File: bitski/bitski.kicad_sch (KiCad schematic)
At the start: 9 parts, among them J2 USB_C_Receptacle_USB2.0_16P, U1 ESP32-S3-MINI-1-N8, U2 BQ25185

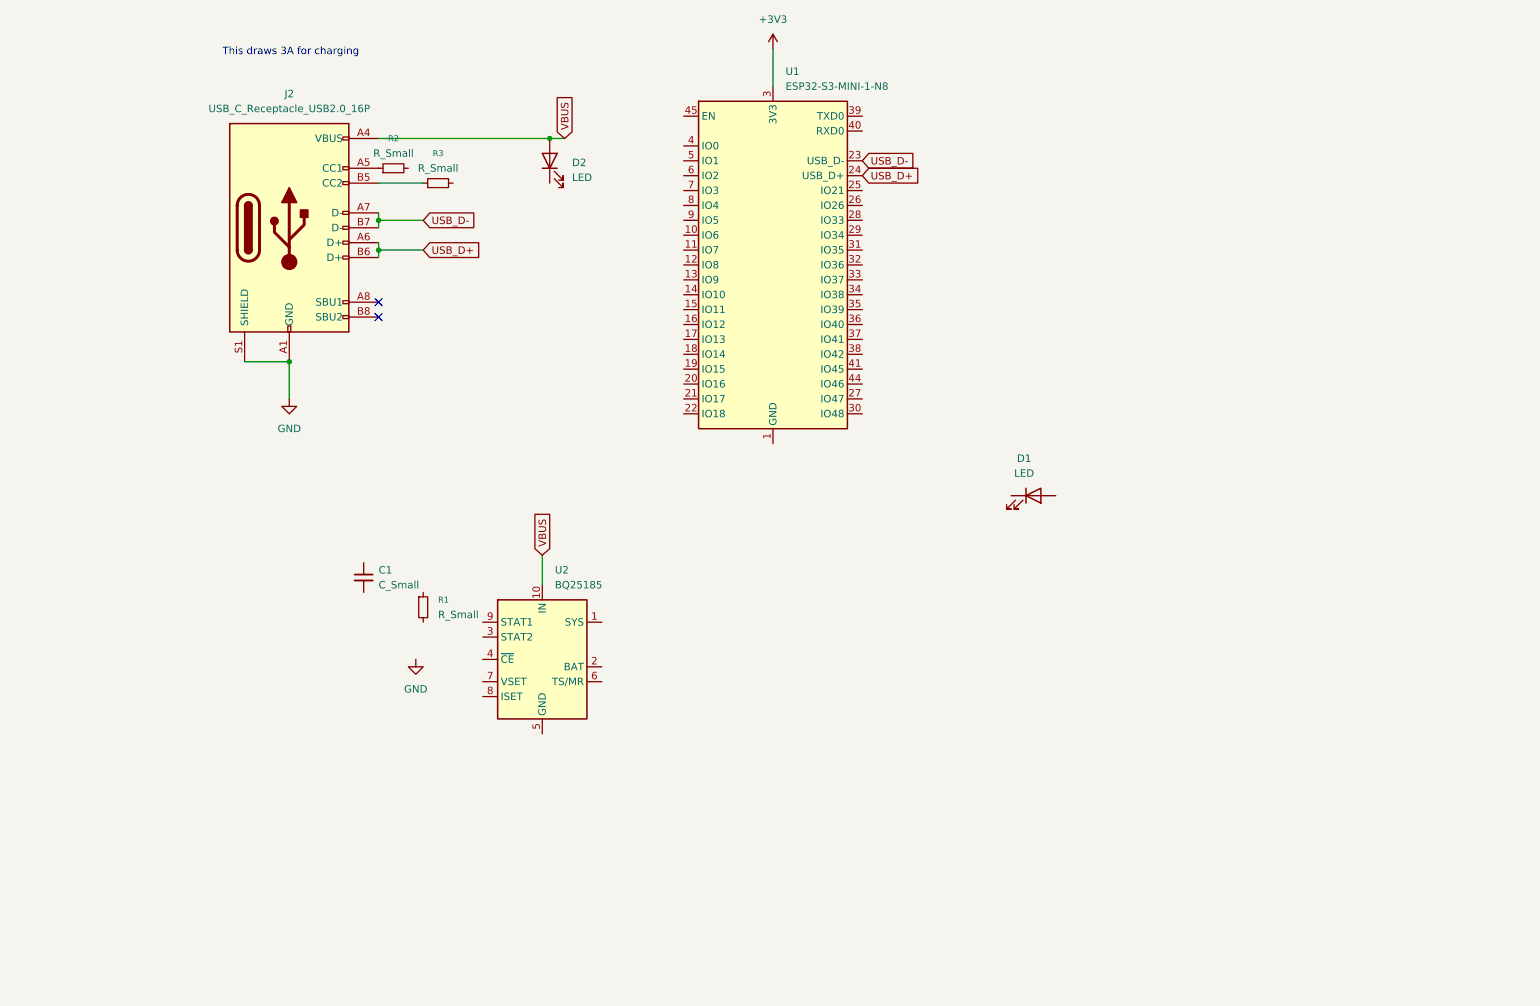
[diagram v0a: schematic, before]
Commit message: updated schematic, added gitignore
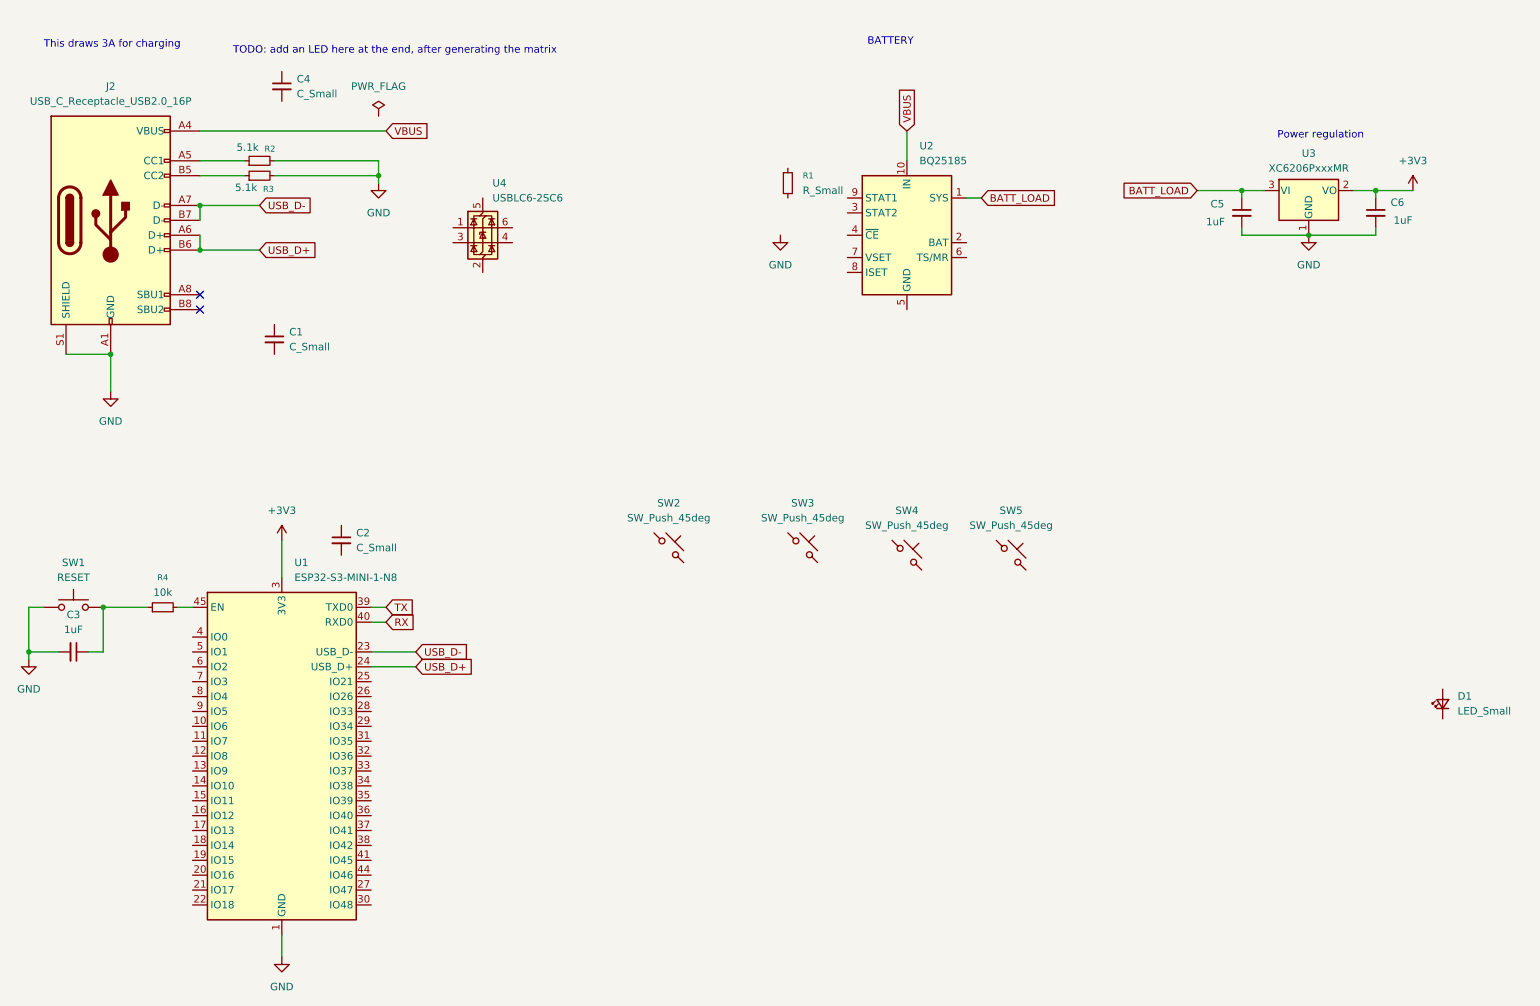
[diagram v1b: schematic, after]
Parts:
- removed D1, D2: LED, symbol Device:LED
- added C2, C4: C_Small, symbol Device:C_Small
- added C3, C5, C6: 1uF, symbol Device:C_Small
- added D1: LED_Small, symbol Device:LED_Small
- added R4: 10k, symbol Device:R_Small
- added SW1: RESET, symbol Switch:SW_Push
- added SW2, SW3, SW4, SW5: SW_Push_45deg, symbol Switch:SW_Push_45deg
- added U3: XC6206PxxxMR, Package_TO_SOT_SMD:SOT-23-3, symbol Regulator_Linear:XC6206PxxxMR
- added U4: USBLC6-2SC6, Package_TO_SOT_SMD:SOT-23-6, symbol Power_Protection:USBLC6-2SC6
- R2, R3: value R_Small -> 5.1k
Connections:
- net +3V3: now also C6.1, U3.2 (VO)
- net GND: now also R2.2, R3.2, U1.1 (GND), U1.2 (GND), U1.42 (GND), U1.43 (GND), U1.46 (GND), U1.47 (GND), U1.48 (GND), U1.49 (GND), U1.50 (GND), U1.51 (GND), U1.52 (GND), U1.53 (GND), U1.54 (GND), U1.55 (GND), U1.56 (GND), U1.57 (GND), U1.58 (GND), U1.59 (GND), U1.60 (GND), U1.61 (GND), U1.62 (GND), U1.63 (GND), U1.64 (GND), U1.65 (GND), C3.2, C5.2, C6.2, SW1.1, U3.1 (GND)
- net TX: now reaches U1.39 (TXD0)
- net RX: now reaches U1.40 (RXD0)
- net at U1.45 (EN): now also R4.2
- net BATT_LOAD: now reaches U2.1 (SYS)
- net BATT_LOAD: now also C5.1, U3.3 (VI)
- new net: C3.1, R4.1, SW1.2
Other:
- note added: "BATTERY"
- note added: "Power regulation"
- note added: "TODO: add an LED here at the end, after generating the matrix"
- moved on the sheet: C1, J2, R1, R2, R3, U1, U2

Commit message: updated board waow
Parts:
- removed C1, C2, C4: C_Small, symbol Device:C_Small
- removed D1: LED_Small, symbol Device:LED_Small
- removed R1: R_Small, symbol Device:R_Small
- removed R2, R3: 5.1k, symbol Device:R_Small
- added C7, C8: 0pF, symbol Device:C_Small
- added D2: D_Schottky, symbol Device:D_Schottky
- added D3, D4, D5, D6: LED_45deg, LED_SMD:LED_0402_1005Metric, symbol Device:LED_45deg
- added J1: Conn_02x20_Odd_Even, symbol Connector_Generic:Conn_02x20_Odd_Even
- added JP1: Jumper_2_Small_Bridged, symbol Jumper:Jumper_2_Small_Bridged
- added R2: 5.1k, Resistor_SMD:R_0402_1005Metric, symbol Device:R
- added R3: 5.1k, symbol Device:R
- added R5, R6: 33, symbol Device:R
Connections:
- net GND: now also SW2.2, SW3.2, SW4.2, SW5.2, U2.5 (GND), U4.2 (GND), C7.2, C8.2, R2.2, R3.2
- net VBUS: now also U4.5 (VBUS), D2.2 (A); no longer U2.10 (IN)
- net USB_DM: now reaches U4.1 (I/O1)
- net USB_DM: now also J2.A7 (D-), J2.B7 (D-)
- net USB_DP: now reaches U4.3 (I/O2)
- net USB_DP: now also J2.A6 (D+), J2.B6 (D+)
- net at U4.4 (I/O2): now also C7.1, R6.1
- net at U4.6 (I/O1): now also C8.1, R5.1
- net at J2.B5 (CC2): now also R3.1
- net at J2.A5 (CC1): now also R2.1
- net INPUT4: now reaches SW5.1
- net INPUT1: now reaches SW2.1
- net INPUT3: now reaches SW4.1
- net INPUT2: now reaches SW3.1
- removed net USB_D+: J2.A6 (D+), J2.B6 (D+), U1.24 (USB_D+)
- removed net USB_D-: J2.A7 (D-), J2.B7 (D-), U1.23 (USB_D-)
- new net +5V: D2.1 (K), U2.10 (IN)
- new net USB_DM_CLEAN: R5.2, U1.23 (USB_D-)
- new net USB_DP_CLEAN: R6.2, U1.24 (USB_D+)
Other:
- note added: "// Break out the remaining pins"
- note added: "LED Grid"
- note added: "This draws 1.5A as per spec"
- note added: "USB"
- note added: "User Inputs!"
- note added: "ts might be cooked"
- note removed: "This draws 3A for charging"
- moved on the sheet: C3, C5, C6, R4, SW1, SW2, SW3, SW4, SW5, U1, U2, U3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

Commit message: more progress
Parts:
- added C1: 10uF, Capacitor_SMD:C_0402_1005Metric, symbol Device:C_Small
- added J3: JST_XH_2.54mm, symbol Connector:Conn_01x02_Socket
- added SW6: ON/OFF, symbol Switch:SW_SPDT
- added TP1: TestPoint, symbol Connector:TestPoint
- added U5: SHT4x, Sensor_Humidity:Sensirion_DFN-4_1.5x1.5mm_P0.8mm_SHT4x_NoCentralPad, symbol Sensor_Humidity:SHT4x
- added U6: BMP280, Package_LGA:Bosch_LGA-8_2x2.5mm_P0.65mm_ClockwisePinNumbering, symbol Sensor_Pressure:BMP280
- C3, C5, C6: footprint (none) -> Capacitor_SMD:C_0402_1005Metric
- C7, C8: footprint (none) -> Capacitor_SMD:C_0603_1608Metric_Pad1.08x0.95mm_HandSolder
- D3: footprint LED_SMD:LED_0402_1005Metric -> Resistor_SMD:R_0402_1005Metric_Pad0.72x0.64mm_HandSolder
- R3, R4, R5, R6: footprint (none) -> Resistor_SMD:R_0402_1005Metric
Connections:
- net +3V3: now also SW6.1 (A); no longer C6.1, U3.2 (VO)
- net BATT_LOAD: now also C1.1
- net +BATT: now reaches U2.2 (BAT)
- net +BATT: now also J3.1 (Pin_1)
- net GND renamed -BATT
- net -BATT: now also C1.2, J3.2 (Pin_2)
- new net: C6.1, SW6.2 (B), U3.2 (VO)
- no-connect marks 2 -> 3
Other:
- note added: "apparently we can hook these up to touch pins?? must try lol"
- note added: "need to change to bmp580 (check datasheet)"
- note added: "using a clone here l0l"
- moved on the sheet: C5, C6, J1, JP1, R5, R6, U2, U3

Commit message: made changes waow
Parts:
- added U7: IS31FL3733-TQ, Package_QFP:TQFP-48-1EP_7x7mm_P0.5mm_EP5x5mm, symbol Driver_LED:IS31FL3733-TQ
- U5: value SHT4x -> GXHT40AD
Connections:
- new net: U7.12 (PGND), U7.5 (PGND)
- new net: U7.48 (GND), U7.49 (GND)
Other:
- note added: "LED Grid, 12x24 0603"
- note added: "This is an SHT40 clone - measures humidity & temp"
- note added: "need to replace this with the 3741 instead"
- note removed: "LED Grid"
- note removed: "ts might be cooked"
- note removed: "using a clone here l0l"
- moved on the sheet: C3, C5, C6, D3, D4, D5, D6, J1, JP1, R4, SW1, SW2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

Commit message: waow updated board
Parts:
- removed J1: Conn_02x20_Odd_Even, symbol Connector_Generic:Conn_02x20_Odd_Even
- removed TP1: TestPoint, symbol Connector:TestPoint
- added J1: Conn_02x12_Odd_Even, symbol Connector_Generic:Conn_02x12_Odd_Even
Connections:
- net +3V3: now also U5.3 (VDD), U6.8 (VDD)
- net -BATT: now also U5.4 (VSS), U6.1 (GND), U6.7 (GND)
- net SHT40_SDA: now reaches U5.1 (SDA)
- net SHT40_SCL: now reaches U5.2 (SCL)
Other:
- note added: "TODO: ADD TESTPOINTS EVERYWHERE"
- note added: "apparently we can hook these up to touch pins?? must try lol ^^ lets not!"
- note added: "need to change to bmp580 (check datasheet) primarily measures barometric pressure, but can also +-0.5C on temp"
- note removed: "apparently we can hook these up to touch pins?? must try lol"
- note removed: "need to change to bmp580 (check datasheet)"
- moved on the sheet: JP1, SW2, SW3, SW4, SW5, U6

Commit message: updates!
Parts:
- removed U7: IS31FL3733-TQ, Package_QFP:TQFP-48-1EP_7x7mm_P0.5mm_EP5x5mm, symbol Driver_LED:IS31FL3733-TQ
- added C2: C_Small, symbol Device:C_Small
- added C4: 100nF, symbol Device:C_Small
- added R1, R7: 10k, symbol Device:R_Small
- added U7, U8: IS31FL3731-QF, Package_DFN_QFN:QFN-28-1EP_4x4mm_P0.4mm_EP2.3x2.3mm, symbol Driver_LED:IS31FL3731-QF
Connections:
- net -BATT is gone; now on net +3V3: C1.2, C3.2, C5.2, C6.2, C7.2, C8.2, J2.A1 (GND), J2.A12 (GND), J2.B1 (GND), J2.B12 (GND), J2.S1 (SHIELD), J3.2 (Pin_2), R2.2, R3.2, SW1.1, SW2.2, SW3.2, SW4.2, SW5.2, U1.1 (GND), U1.2 (GND), U1.42 (GND), U1.43 (GND), U1.46 (GND), U1.47 (GND), U1.48 (GND), U1.49 (GND), U1.50 (GND), U1.51 (GND), U1.52 (GND), U1.53 (GND), U1.54 (GND), U1.55 (GND), U1.56 (GND), U1.57 (GND), U1.58 (GND), U1.59 (GND), U1.60 (GND), U1.61 (GND), U1.62 (GND), U1.63 (GND), U1.64 (GND), U1.65 (GND), U2.5 (GND), U3.1 (GND), U4.2 (GND), U5.4 (VSS), U6.1 (GND), U6.7 (GND)
- net +3V3: now also C2.1, C2.2, C4.1, C4.2, R1.1, R7.1, U8.2 (VCC)
- net SHT40_SCL: now also R1.2
- net SHT40_SDA: now also R7.2
- net INPUT1 renamed USRINPUT1
- net INPUT2 renamed USRINPUT2
- net INPUT3 renamed USRINPUT3
- net INPUT4 renamed USRINPUT4
- new net: U8.29 (GND), U8.5 (GND)
- new net: U7.29 (GND), U7.5 (GND)
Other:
- note added: "double to support everything!"
- note removed: "apparently we can hook these up to touch pins?? must try lol ^^ lets not!"
- note removed: "need to replace this with the 3741 instead"
- moved on the sheet: SW2, SW3, SW4, SW5, U5

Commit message: holy
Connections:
- net SHT40_SCL: now also U1.11 (IO7)
- net SHT40_SDA: now also U1.10 (IO6)
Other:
- moved on the sheet: SW2, SW3, SW4, SW5
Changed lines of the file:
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@@
 	(text "User Inputs!"
 		(exclude_from_sim no)
-		(at 194.564 119.888 0)
+		(at 176.784 122.428 0)
 		(effects
 			(font
@@
 	)
 	(junction
-		(at 199.39 139.7)
+		(at 181.61 142.24)
 		(diameter 0)
 		(color 0 0 0 0)
@@
 	)
 	(junction
-		(at 191.77 139.7)
+		(at 173.99 142.24)
 		(diameter 0)
 		(color 0 0 0 0)
@@
 	)
 	(junction
-		(at 209.55 139.7)
+		(at 191.77 142.24)
 		(diameter 0)
 		(color 0 0 0 0)
@@
 	(wire
 		(pts
-			(xy 199.39 139.7) (xy 199.39 144.78)
+			(xy 181.61 142.24) (xy 181.61 147.32)
 		)
 		(stroke
@@
 	(wire
 		(pts
-			(xy 199.39 139.7) (xy 209.55 139.7)
+			(xy 181.61 142.24) (xy 191.77 142.24)
+		)
+		(stroke
+			(width 0)
+			(type default)
+		)
+	)
+	(wire
+		(pts
+			(xy 45.72 143.51) (xy 49.53 143.51)
 		)
 		(stroke
@@
 	(wire
 		(pts
-			(xy 226.06 139.7) (xy 226.06 135.89)
+			(xy 208.28 142.24) (xy 208.28 138.43)
 		)
 		(stroke
@@
 	(wire
 		(pts
+			(xy 45.72 140.97) (xy 49.53 140.97)
+		)
+		(stroke
+			(width 0)
+			(type default)
+		)
+	)
+	(wire
+		(pts
 			(xy 31.75 269.24) (xy 39.37 269.24)
 		)
@@
 	(wire
 		(pts
-			(xy 173.99 135.89) (xy 173.99 139.7)
+			(xy 156.21 138.43) (xy 156.21 142.24)
 		)
 		(stroke
@@
 	(wire
 		(pts
-			(xy 191.77 135.89) (xy 191.77 139.7)
+			(xy 173.99 138.43) (xy 173.99 142.24)
 		)
 		(stroke
@@
 	(wire
 		(pts
-			(xy 173.99 139.7) (xy 191.77 139.7)
+			(xy 156.21 142.24) (xy 173.99 142.24)
 		)
 		(stroke
@@
 	(wire
 		(pts
-			(xy 191.77 139.7) (xy 199.39 139.7)
+			(xy 173.99 142.24) (xy 181.61 142.24)
 		)
 		(stroke
@@
 	(wire
 		(pts
-			(xy 209.55 139.7) (xy 226.06 139.7)
+			(xy 191.77 142.24) (xy 208.28 142.24)
 		)
 		(stroke
@@
 	(wire
 		(pts
-			(xy 209.55 135.89) (xy 209.55 139.7)
+			(xy 191.77 138.43) (xy 191.77 142.24)
 		)
 		(stroke
@@
 	(global_label "USRINPUT2"
 		(shape input)
-		(at 186.69 130.81 180)
+		(at 168.91 133.35 180)
 		(fields_autoplaced yes)
 		(effects
@@
 		)
 		(property "Intersheetrefs" "${INTERSHEET_REFS}"
-			(at 173.1819 130.81 0)
+			(at 155.4019 133.35 0)
 			(effects
 				(font
@@
 	(global_label "USRINPUT3"
 		(shape input)
-		(at 204.47 130.81 180)
+		(at 186.69 133.35 180)
 		(fields_autoplaced yes)
 		(effects
@@
 		)
 		(property "Intersheetrefs" "${INTERSHEET_REFS}"
-			(at 190.9619 130.81 0)
+			(at 173.1819 133.35 0)
 			(effects
 				(font
@@
 	(global_label "USRINPUT1"
 		(shape input)
-		(at 168.91 130.81 180)
+		(at 151.13 133.35 180)
 		(fields_autoplaced yes)
 		(effects
@@
 		)
 		(property "Intersheetrefs" "${INTERSHEET_REFS}"
-			(at 155.4019 130.81 0)
+			(at 137.6219 133.35 0)
 			(effects
 				(font
@@
 	(global_label "SHT40_SCL"
 		(shape input)
-		(at 102.87 146.05 0)
+		(at 45.72 143.51 180)
 		(fields_autoplaced yes)
 		(effects
@@
 				(size 1.27 1.27)
 			)
-			(justify left)
+			(justify right)
 		)
 		(property "Intersheetrefs" "${INTERSHEET_REFS}"
-			(at 116.257 146.05 0)
+			(at 32.333 143.51 0)
 			(effects
 				(font
 					(size 1.27 1.27)
 				)
-				(justify left)
+				(justify right)
 				(hide yes)
 			)
@@
 	(global_label "SHT40_SDA"
 		(shape input)
-		(at 102.87 140.97 0)
+		(at 45.72 140.97 180)
 		(fields_autoplaced yes)
 		(effects
@@
 				(size 1.27 1.27)
 			)
-			(justify left)
+			(justify right)
 		)
 		(property "Intersheetrefs" "${INTERSHEET_REFS}"
-			(at 116.3175 140.97 0)
+			(at 32.2725 140.97 0)
 			(effects
 				(font
 					(size 1.27 1.27)
 				)
-				(justify left)
+				(justify right)
 				(hide yes)
 			)
@@
 	(global_label "USRINPUT4"
 		(shape input)
-		(at 220.98 130.81 180)
+		(at 203.2 133.35 180)
 		(fields_autoplaced yes)
 		(effects
@@
 		)
 		(property "Intersheetrefs" "${INTERSHEET_REFS}"
-			(at 207.4719 130.81 0)
+			(at 189.6919 133.35 0)
 			(effects
 				(font
@@
 	(symbol
 		(lib_id "Switch:SW_Push_45deg")
-		(at 223.52 133.35 0)
+		(at 205.74 135.89 0)
 		(unit 1)
 		(exclude_from_sim no)
@@
 		(fields_autoplaced yes)
 		(property "Reference" "SW5"
-			(at 223.52 125.73 0)
+			(at 205.74 128.27 0)
 			(effects
 				(font
@@
 		)
 		(property "Value" "SW_Push_45deg"
-			(at 223.52 128.27 0)
+			(at 205.74 130.81 0)
 			(effects
 				(font
@@
 		)
 		(property "Footprint" ""
-			(at 223.52 133.35 0)
+			(at 205.74 135.89 0)
 			(effects
 				(font
@@
 		)
 		(property "Datasheet" "~"
-			(at 223.52 133.35 0)
+			(at 205.74 135.89 0)
 			(effects
 				(font
@@
 		)
 		(property "Description" "Push button switch, normally open, two pins, 45° tilted"
-			(at 223.52 133.35 0)
+			(at 205.74 135.89 0)
 			(effects
 				(font
@@
 	(symbol
 		(lib_id "Switch:SW_Push_45deg")
-		(at 171.45 133.35 0)
+		(at 153.67 135.89 0)
 		(unit 1)
 		(exclude_from_sim no)
@@
 		(fields_autoplaced yes)
 		(property "Reference" "SW2"
-			(at 171.45 125.73 0)
+			(at 153.67 128.27 0)
 			(effects
 				(font
@@
 		)
 		(property "Value" "SW_Push_45deg"
-			(at 171.45 128.27 0)
+			(at 153.67 130.81 0)
 			(effects
 				(font
@@
 		)
 		(property "Footprint" ""
-			(at 171.45 133.35 0)
+			(at 153.67 135.89 0)
 			(effects
 				(font
@@
 		)
 		(property "Datasheet" "~"
-			(at 171.45 133.35 0)
+			(at 153.67 135.89 0)
 			(effects
 				(font
@@
 		)
 		(property "Description" "Push button switch, normally open, two pins, 45° tilted"
-			(at 171.45 133.35 0)
+			(at 153.67 135.89 0)
 			(effects
 				(font
@@
 	(symbol
 		(lib_id "Switch:SW_Push_45deg")
-		(at 207.01 133.35 0)
+		(at 189.23 135.89 0)
 		(unit 1)
 		(exclude_from_sim no)
@@
 		(fields_autoplaced yes)
 		(property "Reference" "SW4"
-			(at 207.01 125.73 0)
+			(at 189.23 128.27 0)
 			(effects
 				(font
@@
 		)
 		(property "Value" "SW_Push_45deg"
-			(at 207.01 128.27 0)
+			(at 189.23 130.81 0)
 			(effects
 				(font
@@
 		)
 		(property "Footprint" ""
-			(at 207.01 133.35 0)
+			(at 189.23 135.89 0)
 			(effects
 				(font
@@
 		)
 		(property "Datasheet" "~"
-			(at 207.01 133.35 0)
+			(at 189.23 135.89 0)
 			(effects
 				(font
@@
 		)
 		(property "Description" "Push button switch, normally open, two pins, 45° tilted"
-			(at 207.01 133.35 0)
+			(at 189.23 135.89 0)
 			(effects
 				(font
@@
 	(symbol
 		(lib_id "Switch:SW_Push_45deg")
-		(at 189.23 133.35 0)
+		(at 171.45 135.89 0)
 		(unit 1)
 		(exclude_from_sim no)
@@
 		(fields_autoplaced yes)
 		(property "Reference" "SW3"
-			(at 189.23 125.73 0)
+			(at 171.45 128.27 0)
 			(effects
 				(font
@@
 		)
 		(property "Value" "SW_Push_45deg"
-			(at 189.23 128.27 0)
+			(at 171.45 130.81 0)
 			(effects
 				(font
@@
 		)
 		(property "Footprint" ""
-			(at 189.23 133.35 0)
+			(at 171.45 135.89 0)
 			(effects
 				(font
@@
 		)
 		(property "Datasheet" "~"
-			(at 189.23 133.35 0)
+			(at 171.45 135.89 0)
 			(effects
 				(font
@@
 		)
 		(property "Description" "Push button switch, normally open, two pins, 45° tilted"
-			(at 189.23 133.35 0)
+			(at 171.45 135.89 0)
 			(effects
 				(font
@@
 	(symbol
 		(lib_id "power:GND")
-		(at 199.39 144.78 0)
+		(at 181.61 147.32 0)
 		(unit 1)
 		(exclude_from_sim no)
@@
 		(fields_autoplaced yes)
 		(property "Reference" "#PWR015"
-			(at 199.39 151.13 0)
+			(at 181.61 153.67 0)
 			(effects
 				(font
@@
 		)
 		(property "Value" "GND"
-			(at 199.39 149.86 0)
+			(at 181.61 152.4 0)
 			(effects
 				(font
@@
 		)
 		(property "Footprint" ""
-			(at 199.39 144.78 0)
+			(at 181.61 147.32 0)
 			(effects
 				(font
@@
 		)
 		(property "Datasheet" ""
-			(at 199.39 144.78 0)
+			(at 181.61 147.32 0)
 			(effects
 				(font
@@
 		)
 		(property "Description" "Power symbol creates a global label with name \"GND\" , ground"
-			(at 199.39 144.78 0)
+			(at 181.61 147.32 0)
 			(effects
 				(font
